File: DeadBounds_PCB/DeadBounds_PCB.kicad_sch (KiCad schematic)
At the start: 0 parts

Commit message: Test
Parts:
- added U1: MSPM0G3507SPMR, symbol DeadBounds_Symbols:MSPM0G3507SPMR
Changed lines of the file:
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@@
 	(generator_version "10.0")
 	(paper "A4")
+	(symbol
+		(lib_id "DeadBounds_Symbols:MSPM0G3507SPMR")
+		(at 115.57 25.4 0)
+		(unit 1)
+		(body_style 1)
+		(exclude_from_sim no)
+		(in_bom yes)
+		(on_board no)
+		(in_pos_files yes)
+		(dnp no)
+		(fields_autoplaced yes)
+		(property "Reference" "U1"
+			(at 148.5392 129.54 0)
+			(show_name no)
+			(do_not_autoplace no)
+			(effects
+				(font
+					(size 1.524 1.524)
+				)
+			)
+		)
+		(property "Value" "MSPM0G3507SPMR"
+			(at 148.5392 132.08 0)
+			(show_name no)
+			(do_not_autoplace no)
+			(effects
+				(font
+					(size 1.524 1.524)
+				)
+			)
+		)
+		(property "Footprint" ""
+			(at 165.354 14.732 0)
+			(hide yes)
+			(show_name no)
+			(do_not_autoplace no)
+			(effects
+				(font
+					(size 1.27 1.27)
+					(italic yes)
+				)
+			)
+		)
+		(property "Datasheet" ""
+			(at 135.382 2.032 0)
+			(hide yes)
+			(show_name no)
+			(do_not_autoplace no)
+			(effects
+				(font
+					(size 1.27 1.27)
+					(italic yes)
+				)
+			)
+		)
+		(property "Description" ""
+			(at 115.57 25.4 0)
+			(hide yes)
+			(show_name no)
+			(do_not_autoplace no)
+			(effects
+				(font
+					(size 1.27 1.27)
+				)
+			)
+		)
+		(pin "3"
+		)
+		(pin "18"
+		)
+		(pin "9"
+		)
+		(pin "12"
+		)
+		(pin "13"
+		)
+		(pin "15"
+		)
+		(pin "14"
+		)
+		(pin "6"
+		)
+		(pin "17"
+		)
+		(pin "7"
+		)
+		(pin "25"
+		)
+		(pin "2"
+		)
+		(pin "10"
+		)
+		(pin "11"
+		)
+		(pin "5"
+		)
+		(pin "16"
+		)
+		(pin "21"
+		)
+		(pin "23"
+		)
+		(pin "1"
+		)
+		(pin "19"
+		)
+		(pin "8"
+		)
+		(pin "24"
+		)
+		(pin "31"
+		)
+		(pin "4"
+		)
+		(pin "27"
+		)
+		(pin "47"
+		)
+		(pin "20"
+		)
+		(pin "29"
+		)
+		(pin "40"
+		)
+		(pin "33"
+		)
+		(pin "44"
+		)
+		(pin "35"
+		)
+		(pin "37"
+		)
+		(pin "22"
+		)
+		(pin "38"
+		)
+		(pin "39"
+		)
+		(pin "41"
+		)
+		(pin "42"
+		)
+		(pin "45"
+		)
+		(pin "32"
+		)
+		(pin "46"
+		)
+		(pin "58"
+		)
+		(pin "64"
+		)
+		(pin "30"
+		)
+		(pin "28"
+		)
+		(pin "26"
+		)
+		(pin "34"
+		)
+		(pin "36"
+		)
+		(pin "43"
+		)
+		(pin "52"
+		)
+		(pin "54"
+		)
+		(pin "57"
+		)
+		(pin "60"
+		)
+		(pin "55"
+		)
+		(pin "53"
+		)
+		(pin "59"
+		)
+		(pin "62"
+		)
+		(pin "51"
+		)
+		(pin "49"
+		)
+		(pin "50"
+		)
+		(pin "56"
+		)
+		(pin "61"
+		)
+		(pin "63"
+		)
+		(pin "48"
+		)
+		(instances
+			(project "DeadBounds_PCB"
+				(path "/c652495f-dd42-4f45-9891-1e05b67942c0"
+					(reference "U1")
+					(unit 1)
+				)
+			)
+		)
+	)
 	(sheet_instances
 		(path "/"

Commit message: Test 2
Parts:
- added U2: LM3914N, Package_DIP:DIP-18_W7.62mm, symbol Driver_LED:LM3914N
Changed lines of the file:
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@@
+		)
+	)
+	(symbol
+		(lib_id "Driver_LED:LM3914N")
+		(at 48.26 121.92 0)
+		(unit 1)
+		(body_style 1)
+		(exclude_from_sim no)
+		(in_bom yes)
+		(on_board yes)
+		(in_pos_files yes)
+		(dnp no)
+		(fields_autoplaced yes)
+		(property "Reference" "U2"
+			(at 50.4033 104.14 0)
+			(show_name no)
+			(do_not_autoplace no)
+			(effects
+				(font
+					(size 1.27 1.27)
+				)
+				(justify left)
+			)
+		)
+		(property "Value" "LM3914N"
+			(at 50.4033 106.68 0)
+			(show_name no)
+			(do_not_autoplace no)
+			(effects
+				(font
+					(size 1.27 1.27)
+				)
+				(justify left)
+			)
+		)
+		(property "Footprint" "Package_DIP:DIP-18_W7.62mm"
+			(at 48.26 121.92 0)
+			(hide yes)
+			(show_name no)
+			(do_not_autoplace no)
+			(effects
+				(font
+					(size 1.27 1.27)
+				)
+			)
+		)
+		(property "Datasheet" "https://www.ti.com/lit/ds/symlink/lm3914.pdf"
+			(at 48.26 121.92 0)
+			(hide yes)
+			(show_name no)
+			(do_not_autoplace no)
+			(effects
+				(font
+					(size 1.27 1.27)
+				)
+			)
+		)
+		(property "Description" "10 LED Dot/Bar Display Driver, DIP-18"
+			(at 48.26 121.92 0)
+			(hide yes)
+			(show_name no)
+			(do_not_autoplace no)
+			(effects
+				(font
+					(size 1.27 1.27)
+				)
+			)
+		)
+		(pin "6"
+		)
+		(pin "10"
+		)
+		(pin "1"
+		)
+		(pin "4"
+		)
+		(pin "8"
+		)
+		(pin "13"
+		)
+		(pin "14"
+		)
+		(pin "2"
+		)
+		(pin "5"
+		)
+		(pin "7"
+		)
+		(pin "15"
+		)
+		(pin "9"
+		)
+		(pin "16"
+		)
+		(pin "11"
+		)
+		(pin "3"
+		)
+		(pin "17"
+		)
+		(pin "12"
+		)
+		(pin "18"
+		)
+		(instances
+			(project "DeadBounds_PCB"
+				(path "/c652495f-dd42-4f45-9891-1e05b67942c0"
+					(reference "U2")
+					(unit 1)
+				)
+			)
 		)
 	)

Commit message: Setup Schematic Sections
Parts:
- added LCD1: (no value), symbol DeadBounds_Symbols:HiLetgo_ST7735
- added U3: LM3914N, Package_DIP:DIP-18_W7.62mm, symbol Driver_LED:LM3914N
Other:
- note added: "6-Bit DAC"
- note added: "HiLetGo 160 x 128 LCD"
- note added: "Joystick ADCs + Buttons"
- note added: "LED Bar Drivers"
- note added: "MSPM0 MCU"
- moved on the sheet: U1, U2

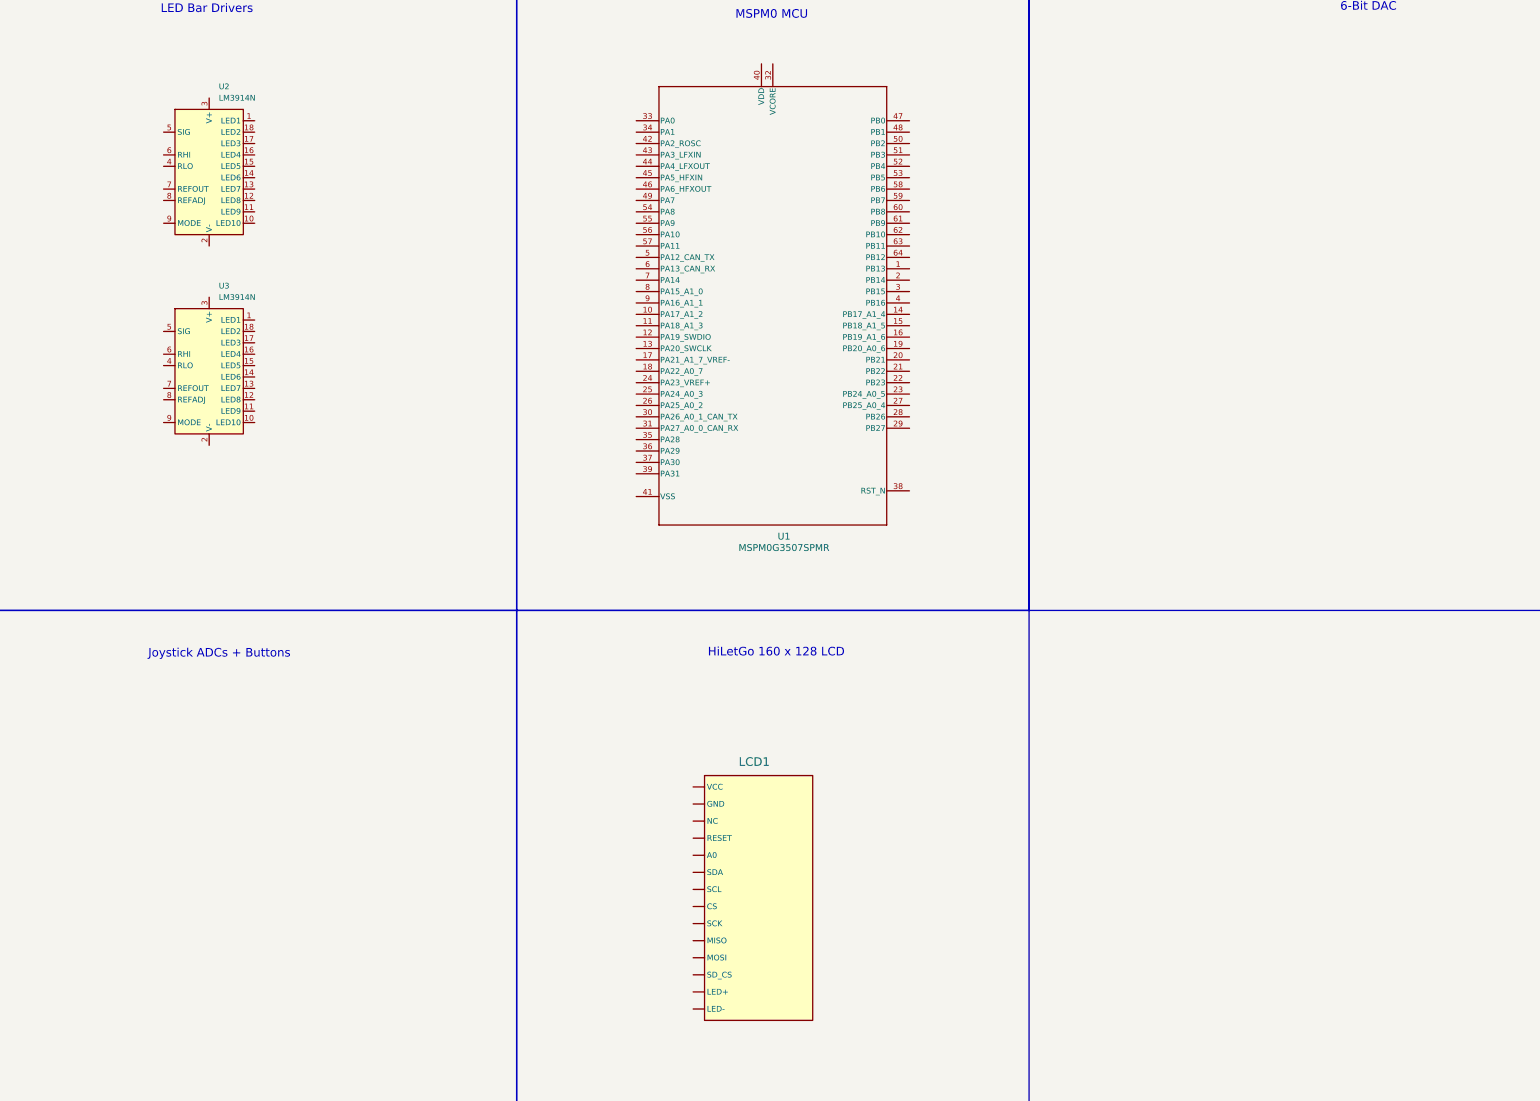
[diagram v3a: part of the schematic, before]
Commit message: Added Hierarchal Sheets
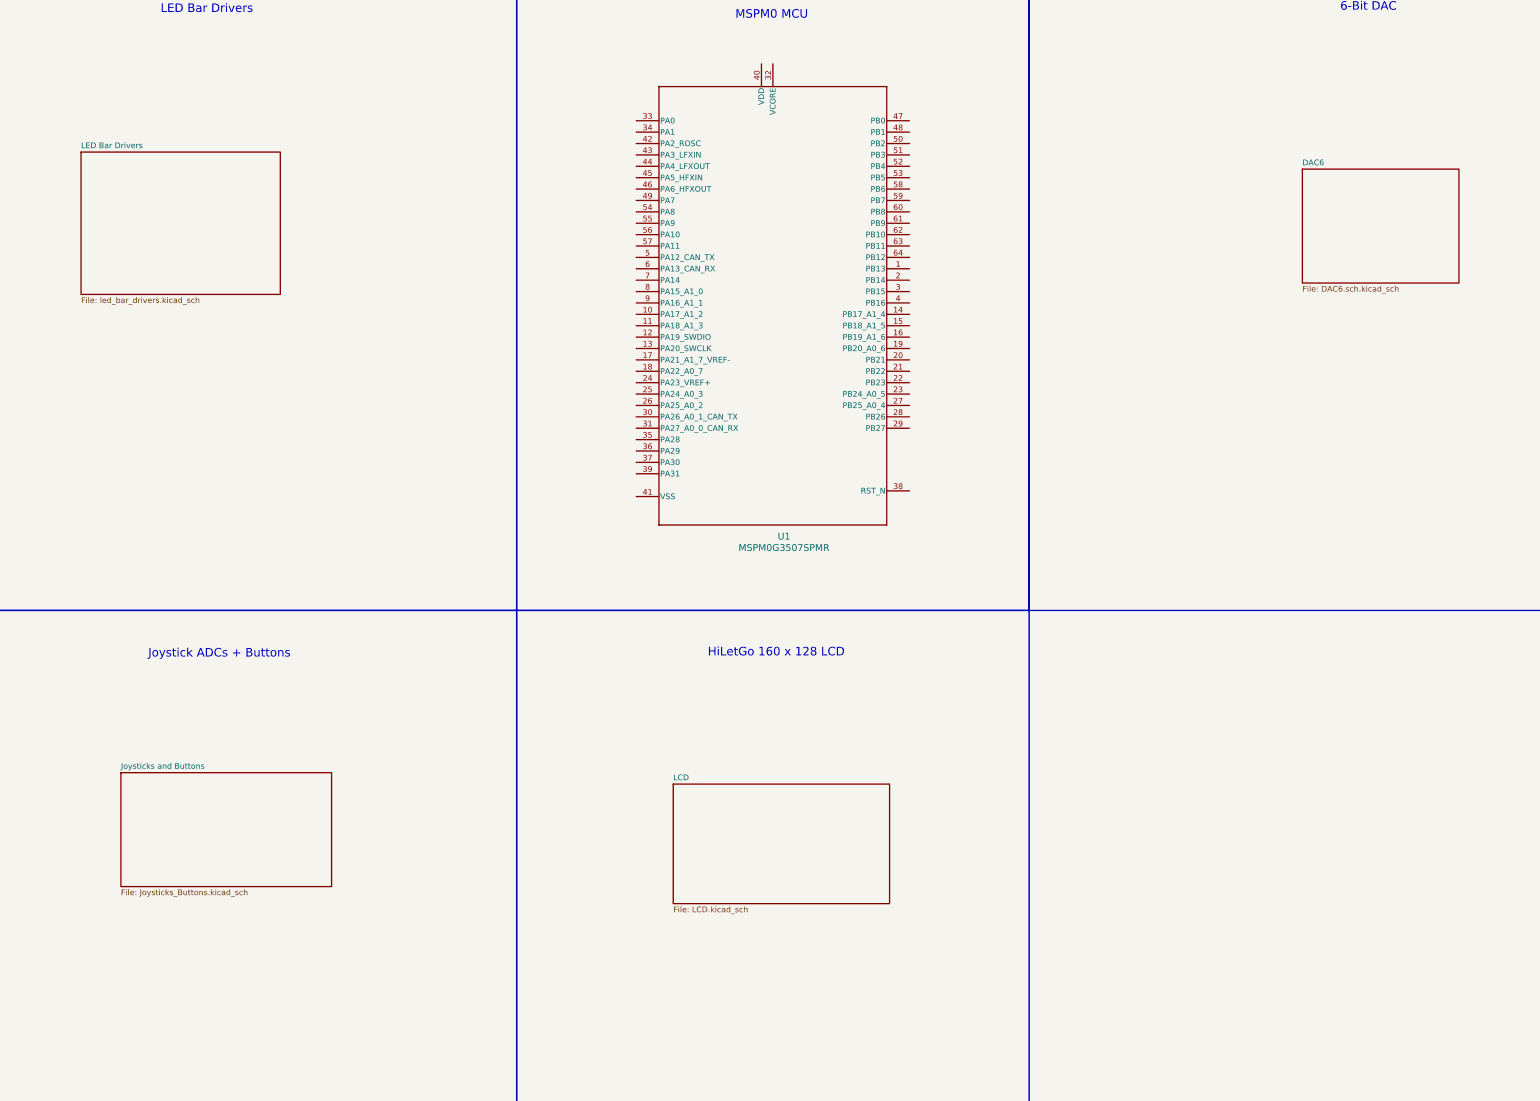
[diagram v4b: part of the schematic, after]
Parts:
- removed LCD1: (no value), symbol DeadBounds_Symbols:HiLetgo_ST7735
- removed U2, U3: LM3914N, Package_DIP:DIP-18_W7.62mm, symbol Driver_LED:LM3914N
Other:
- added sheet DAC6 (DAC6.sch.kicad_sch)
- added sheet Joysticks and Buttons (Joysticks_Buttons.kicad_sch)
- added sheet LCD (LCD.kicad_sch)
- added sheet LED Bar Drivers (led_bar_drivers.kicad_sch)

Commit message: Finished schematics, assigned/made footprints except for resistors
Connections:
- net LCD/RESET_LCD: now reaches U1.3 (PB15)
- net Joysticks and Buttons/VRY1: now reaches U1.30 (PA26_A0_1_CAN_TX)
- net Joysticks and Buttons/VRX1: now reaches U1.31 (PA27_A0_0_CAN_RX)
- net DAC6/LS1DAC0: now reaches U1.47 (PB0)
- net DAC6/LS1DAC1: now reaches U1.48 (PB1)
- net DAC6/LS1DAC2: now reaches U1.50 (PB2)
- net DAC6/LS1DAC3: now reaches U1.51 (PB3)
- net DAC6/LS1DAC4: now reaches U1.52 (PB4)
- net DAC6/LS1DAC5: now reaches U1.53 (PB5)
- net LCD/CS_LCD: now reaches U1.58 (PB6)
- net D/C_LCD: now reaches U1.6 (PA13_CAN_RX)
- net LCD/MOSI_LCD: now reaches U1.60 (PB8)
- net LCD/CLK_LCD: now reaches U1.61 (PB9)
- net Joysticks and Buttons/VRX2: now reaches U1.8 (PA15_A1_0)
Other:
- sheet DAC6 ports: added LS1DAC0, LS1DAC1, LS1DAC2, LS1DAC3, LS1DAC4, LS1DAC5; removed none
- sheet Joysticks and Buttons ports: added SWLang, SWShoot, VRX1, VRX2, VRY1; removed none
- sheet LCD ports: added CLK_LCD, CS_LCD, D/C_LCD, MOSI_LCD, RESET_LCD; removed none
- sheet LED Bar Drivers ports: added AMMODAC0, AMMODAC1, AMMODAC2, HPDAC0, HPDAC1, HPDAC2, HPDAC3; removed none
- note added: "Audio 6-bit DAC"
- note removed: "6-Bit DAC"
- note removed: "HiLetGo 160 x 128 LCD"
- note removed: "Joystick ADCs + Buttons"
- note removed: "LED Bar Drivers"

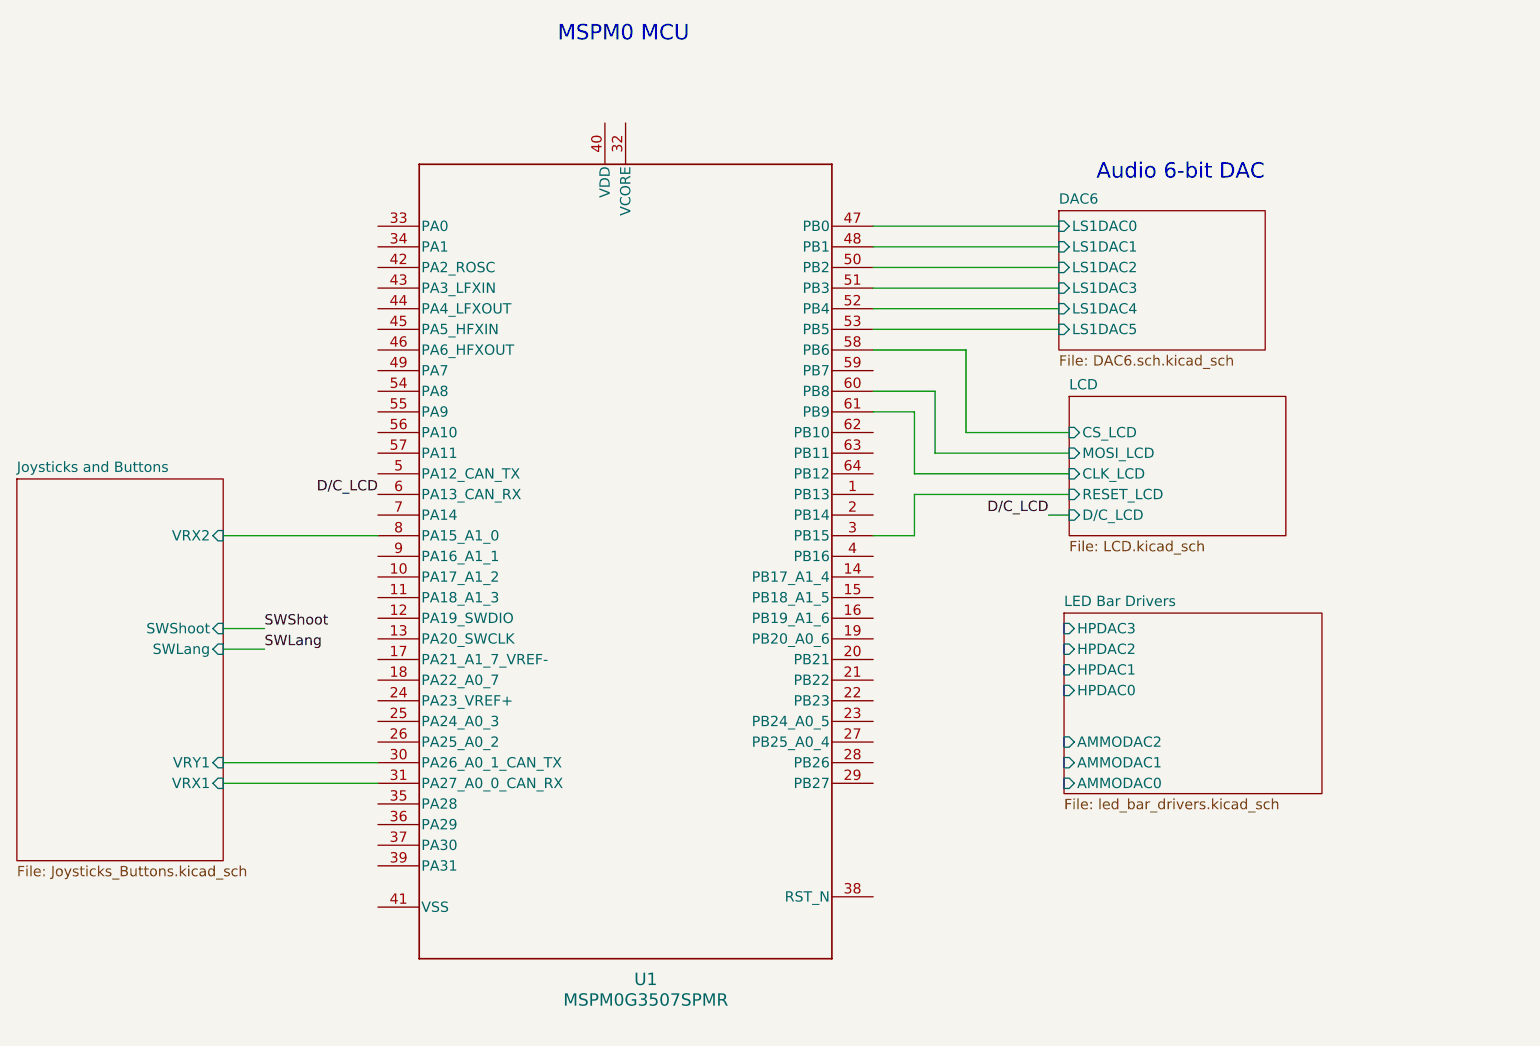
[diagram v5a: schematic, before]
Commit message: MCU wiring and LED resistance edits
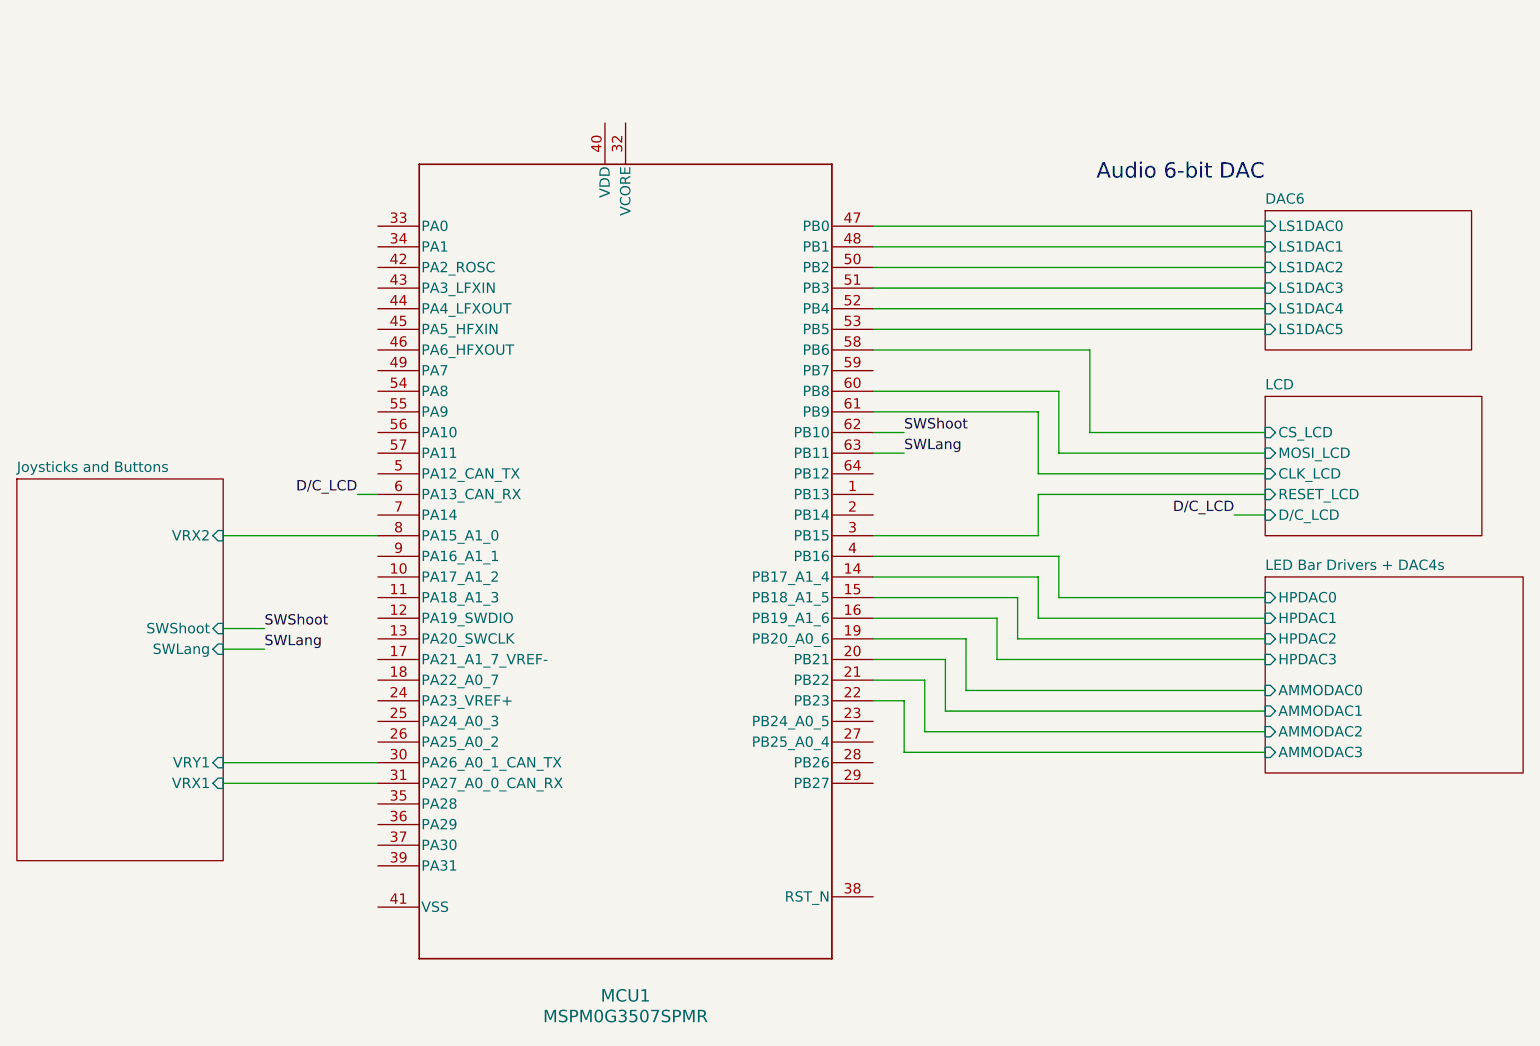
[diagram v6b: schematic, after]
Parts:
- renumbered U1 to MCU1
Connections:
- net LED Bar Drivers + DAC4s/AMMODAC0: now also MCU1.19 (PB20_A0_6)
- net LED Bar Drivers + DAC4s/AMMODAC1: now also MCU1.20 (PB21)
- net LED Bar Drivers + DAC4s/AMMODAC2: now also MCU1.21 (PB22)
- net LED Bar Drivers + DAC4s/HPDAC0: now also MCU1.4 (PB16)
- net LED Bar Drivers + DAC4s/HPDAC1: now also MCU1.14 (PB17_A1_4)
- net LED Bar Drivers + DAC4s/HPDAC2: now also MCU1.15 (PB18_A1_5)
- net LED Bar Drivers + DAC4s/HPDAC3: now also MCU1.16 (PB19_A1_6)
- net SWLang: now also MCU1.63 (PB11)
- net SWShoot: now also MCU1.62 (PB10)
- net LED Bar Drivers + DAC4s/AMMODAC3: now reaches MCU1.22 (PB23)
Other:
- sheet LED Bar Drivers renamed LED Bar Drivers + DAC4s
- sheet LED Bar Drivers + DAC4s ports: added AMMODAC3; removed none
- note removed: "MSPM0 MCU"
